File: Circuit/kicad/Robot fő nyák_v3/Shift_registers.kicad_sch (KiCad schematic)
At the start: 3 parts, among them U18 74HC595, U50 74HC595, U55 74HC595

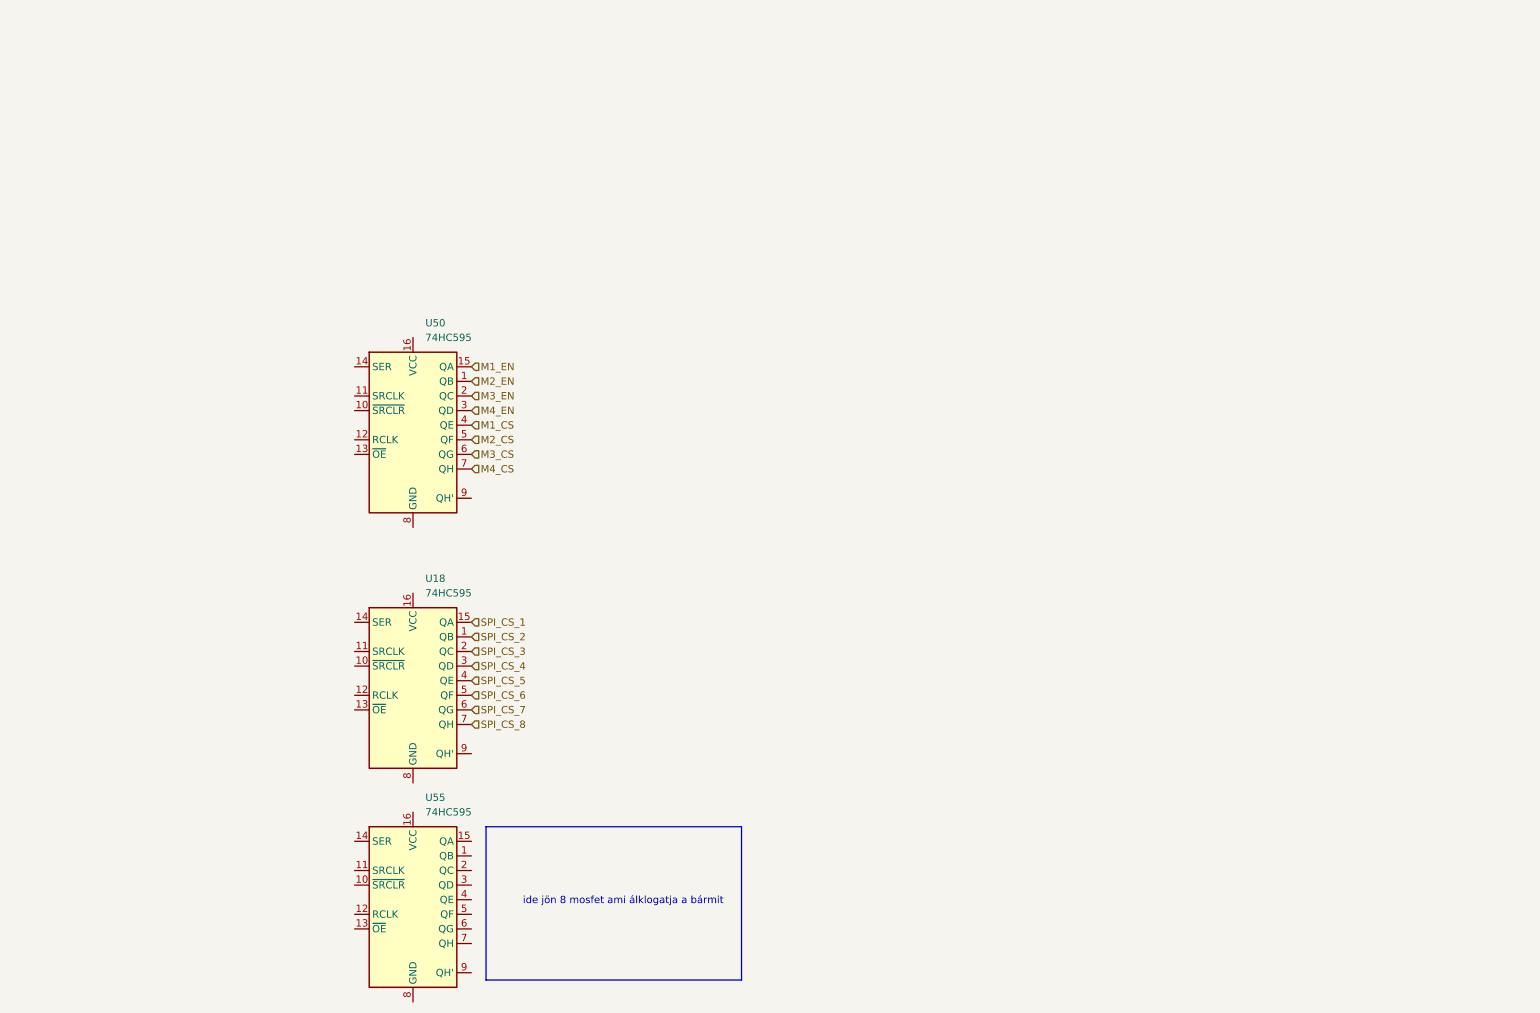
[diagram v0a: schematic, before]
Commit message: KICAD V3.01 Cleaned sheets + update + szekér modell add
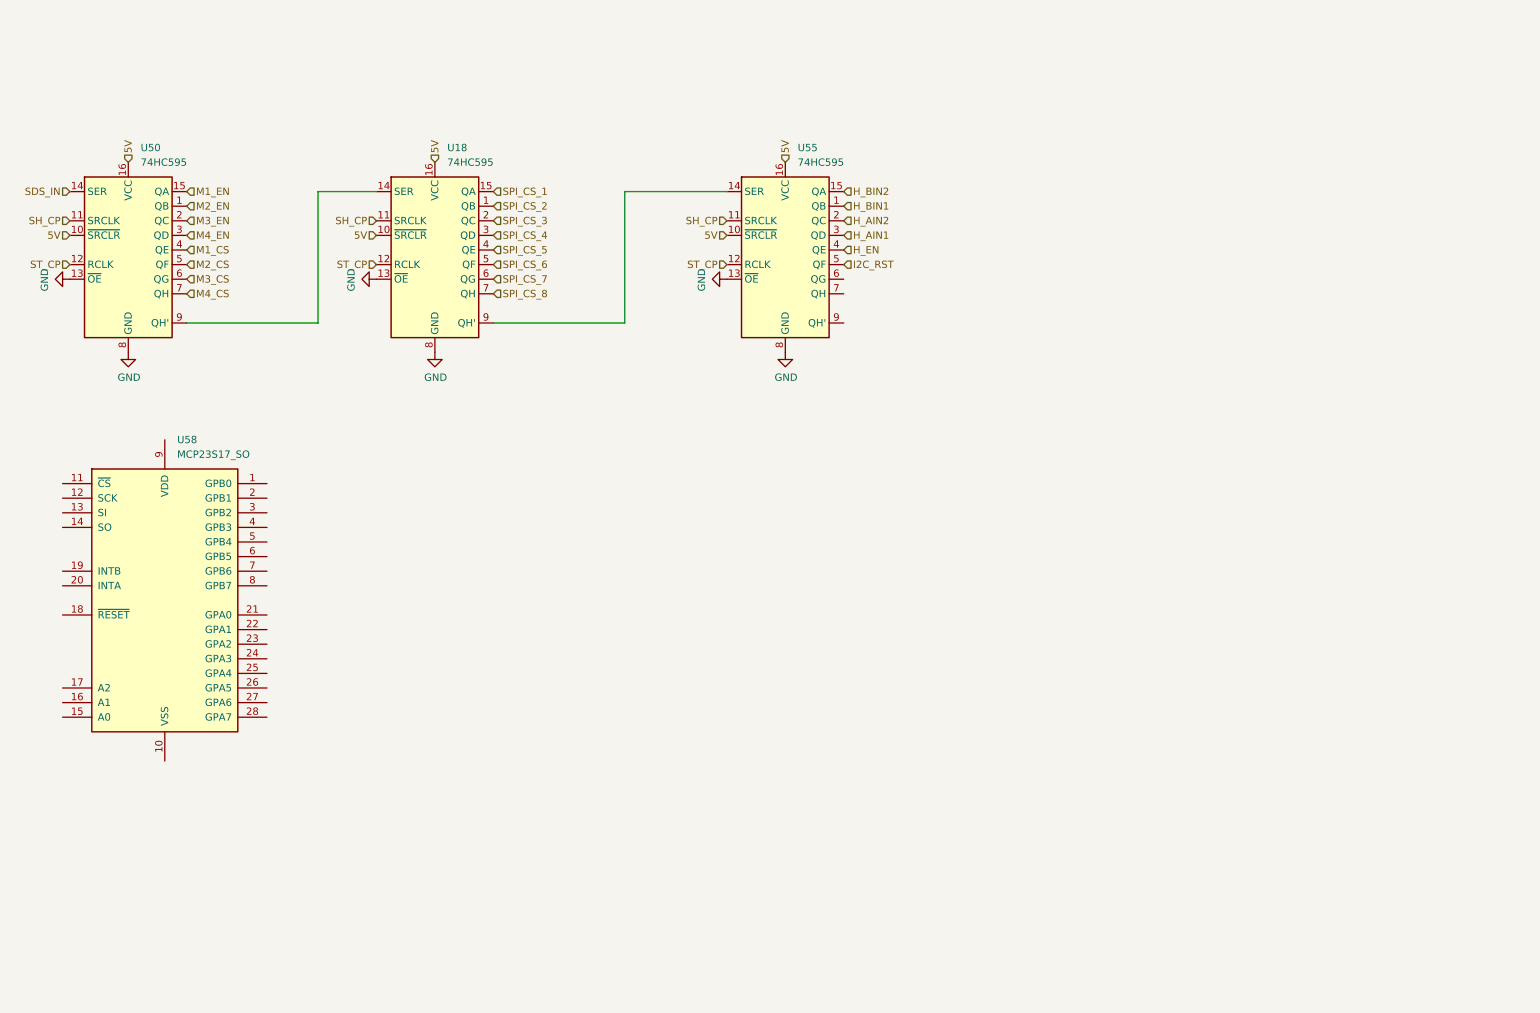
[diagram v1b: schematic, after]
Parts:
- added U58: MCP23S17_SO, Package_SO:SOIC-28W_7.5x17.9mm_P1.27mm, symbol Interface_Expansion:MCP23S17_SO
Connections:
- net H_BIN1: now reaches U55.1 (QB)
- net 5V: now reaches U55.10 (~{SRCLR})
- net 5V: now also U18.10 (~{SRCLR}), U18.16 (VCC), U50.10 (~{SRCLR}), U50.16 (VCC), U55.16 (VCC)
- net SH_CP: now reaches U55.11 (SRCLK)
- net SH_CP: now also U18.11 (SRCLK), U50.11 (SRCLK)
- net ST_CP: now reaches U55.12 (RCLK)
- net ST_CP: now also U18.12 (RCLK), U50.12 (RCLK)
- net GND: now reaches U55.13 (~{OE})
- net GND: now also U18.13 (~{OE}), U18.8 (GND), U50.13 (~{OE}), U50.8 (GND), U55.8 (GND)
- net at U55.14 (SER): now also U18.9 (QH')
- net H_BIN2: now reaches U55.15 (QA)
- net H_AIN2: now reaches U55.2 (QC)
- net H_AIN1: now reaches U55.3 (QD)
- net H_EN: now reaches U55.4 (QE)
- net I2C_RST: now reaches U55.5 (QF)
- net at U18.14 (SER): now also U50.9 (QH')
- net SDS_IN: now reaches U50.14 (SER)
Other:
- note removed: "ide jön 8 mosfet ami álklogatja a bármit"
- moved on the sheet: U18, U50, U55

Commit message: Kicad update: power rails v1.0, todo: hc-sr-04  as6500 ic review shift registers change to MCP23S17_SO
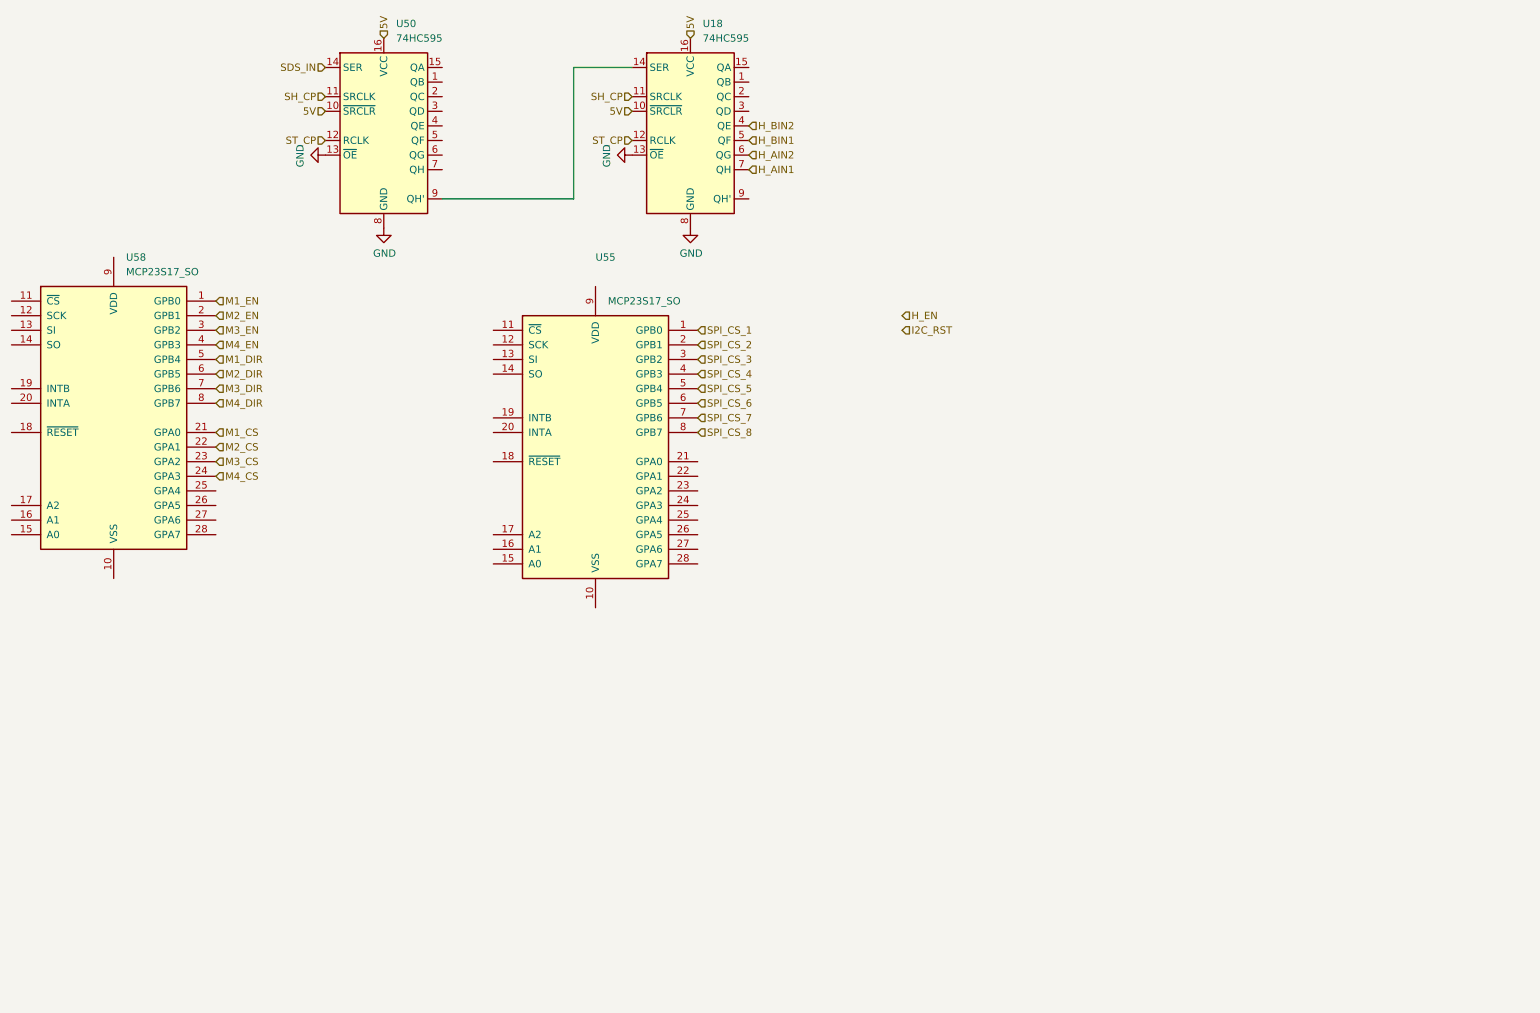
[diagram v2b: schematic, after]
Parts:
- removed U55: 74HC595, symbol 74xx:74HC595
- added U55: MCP23S17_SO, Package_SO:SOIC-28W_7.5x17.9mm_P1.27mm, symbol Interface_Expansion:MCP23S17_SO
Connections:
- net H_AIN1: now also U18.7 (QH)
- net H_AIN2: now also U18.6 (QG)
- net H_BIN1: now also U18.5 (QF)
- net H_BIN2: now also U18.4 (QE)
- net M1_CS: now also U58.21 (GPA0); no longer U50.4 (QE)
- net M1_EN: now also U58.1 (GPB0); no longer U50.15 (QA)
- net M2_CS: now also U58.22 (GPA1); no longer U50.5 (QF)
- net M2_EN: now also U58.2 (GPB1); no longer U50.1 (QB)
- net M3_CS: now also U58.23 (GPA2); no longer U50.6 (QG)
- net M3_EN: now also U58.3 (GPB2); no longer U50.2 (QC)
- net M4_CS: now also U58.24 (GPA3); no longer U50.7 (QH)
- net M4_EN: now also U58.4 (GPB3); no longer U50.3 (QD)
- net SPI_CS_1: now also U55.1 (GPB0); no longer U18.15 (QA)
- net SPI_CS_2: now also U55.2 (GPB1); no longer U18.1 (QB)
- net SPI_CS_3: now also U55.3 (GPB2); no longer U18.2 (QC)
- net SPI_CS_4: now also U55.4 (GPB3); no longer U18.3 (QD)
- net SPI_CS_5: now also U55.5 (GPB4); no longer U18.4 (QE)
- net SPI_CS_6: now also U55.6 (GPB5); no longer U18.5 (QF)
- net SPI_CS_7: now also U55.7 (GPB6); no longer U18.6 (QG)
- net SPI_CS_8: now also U55.8 (GPB7); no longer U18.7 (QH)
- net M1_DIR: now reaches U58.5 (GPB4)
- net M2_DIR: now reaches U58.6 (GPB5)
- net M3_DIR: now reaches U58.7 (GPB6)
- net M4_DIR: now reaches U58.8 (GPB7)
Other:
- moved on the sheet: U18, U50, U58

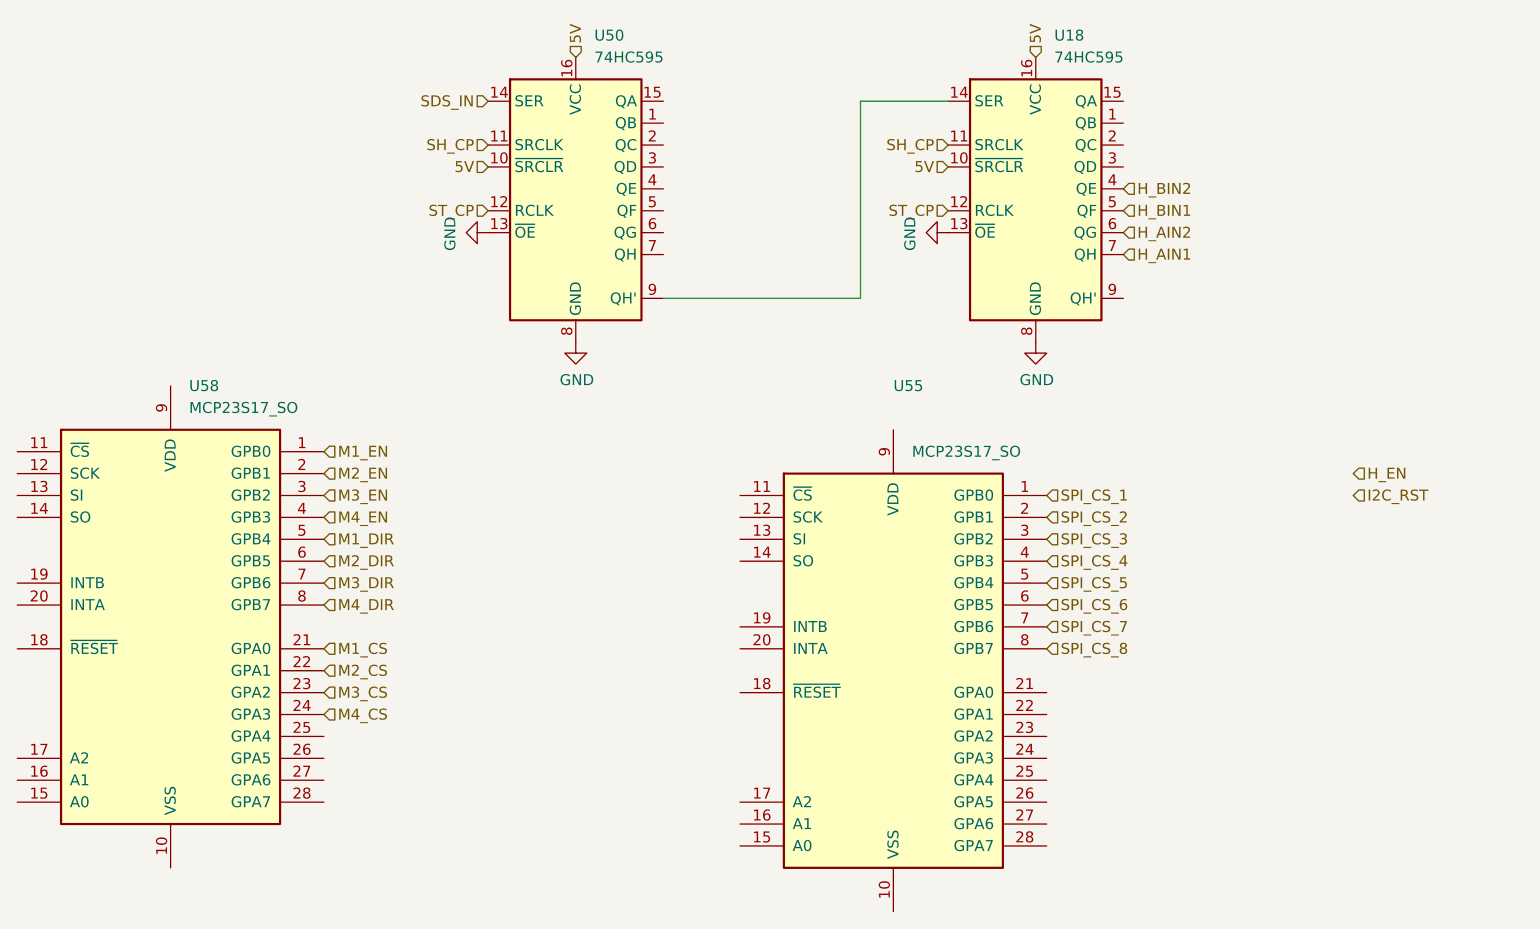
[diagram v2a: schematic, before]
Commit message: kicad v0.1 footprint- assing spi finish
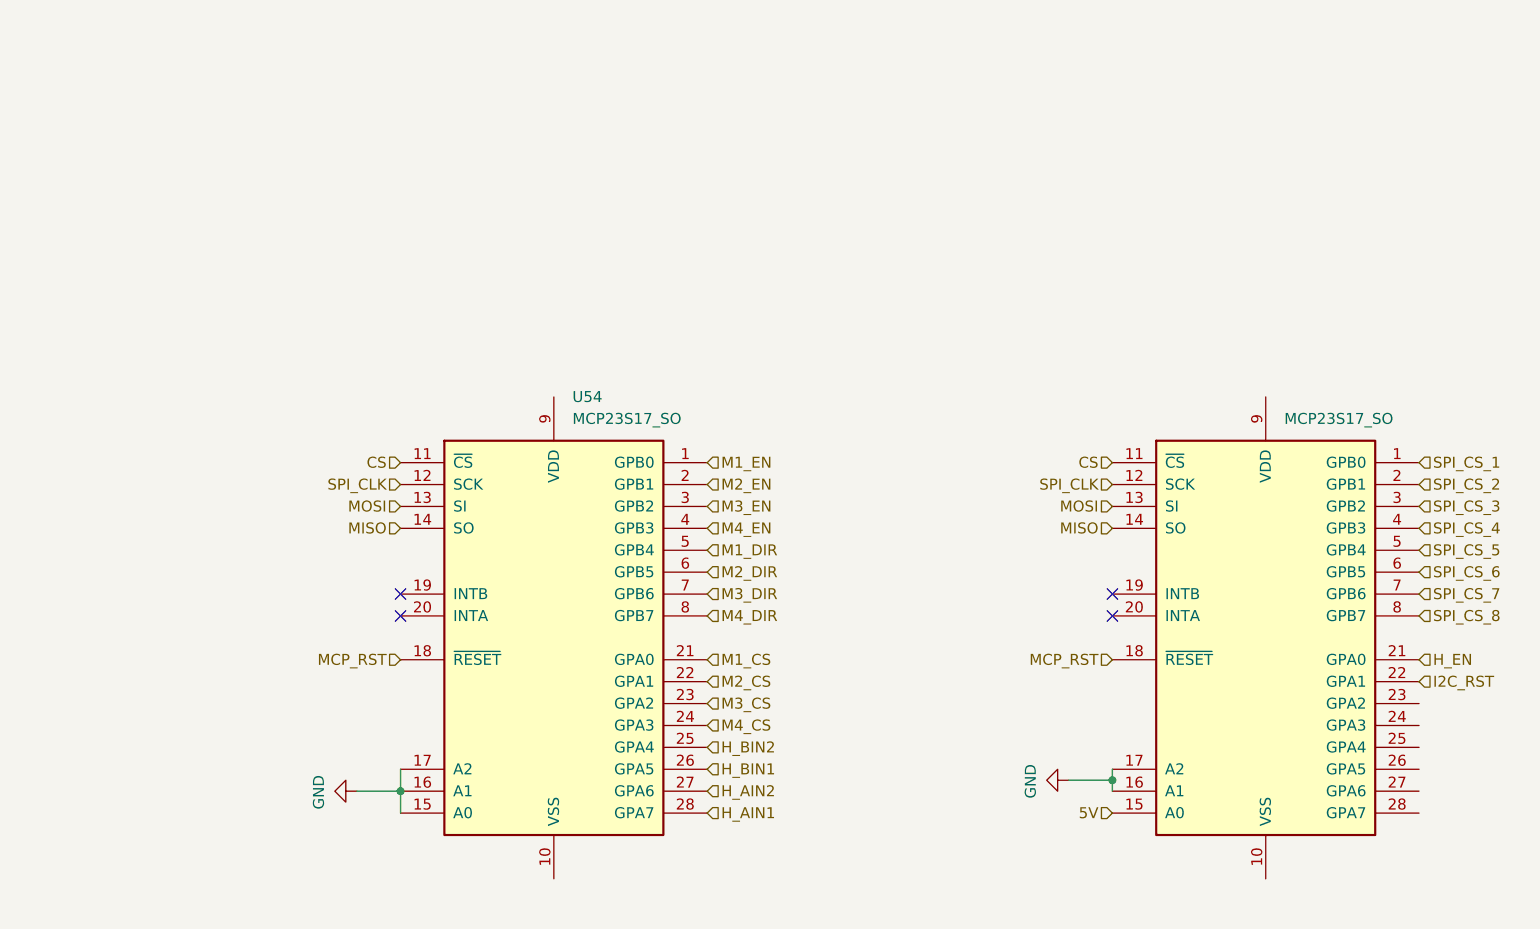
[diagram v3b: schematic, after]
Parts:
- removed U18, U50: 74HC595, symbol 74xx:74HC595
- renumbered U58 to U54
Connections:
- net 5V: now also U55.15 (A0)
- net GND: now also U54.15 (A0), U54.16 (A1), U54.17 (A2), U55.16 (A1), U55.17 (A2)
- net H_AIN1: now also U54.28 (GPA7)
- net H_AIN2: now also U54.27 (GPA6)
- net H_BIN1: now also U54.26 (GPA5)
- net H_BIN2: now also U54.25 (GPA4)
- net H_EN: now also U55.21 (GPA0)
- net I2C_RST: now also U55.22 (GPA1)
- net CS: now reaches U55.11 (~{CS})
- net CS: now also U54.11 (~{CS})
- net SPI_CLK: now reaches U55.12 (SCK)
- net SPI_CLK: now also U54.12 (SCK)
- net MOSI: now reaches U55.13 (SI)
- net MOSI: now also U54.13 (SI)
- net MISO: now reaches U55.14 (SO)
- net MISO: now also U54.14 (SO)
- net MCP_RST: now reaches U55.18 (~{RESET})
- net MCP_RST: now also U54.18 (~{RESET})
- no-connect marks 0 -> 4
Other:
- moved on the sheet: U54
